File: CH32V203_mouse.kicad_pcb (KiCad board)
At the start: 2 copper layers, 30 parts, among them J1 USB_C_Receptacle_USB2.0_16P_u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, J2 Conn_01x05_Pin, J3 Conn_01x04_Pin, SW1 SW_Push, U1 CH32V203G6U6, U2 USBLC6-2SC6, U3 XC6206P332MR, X1 16MHz

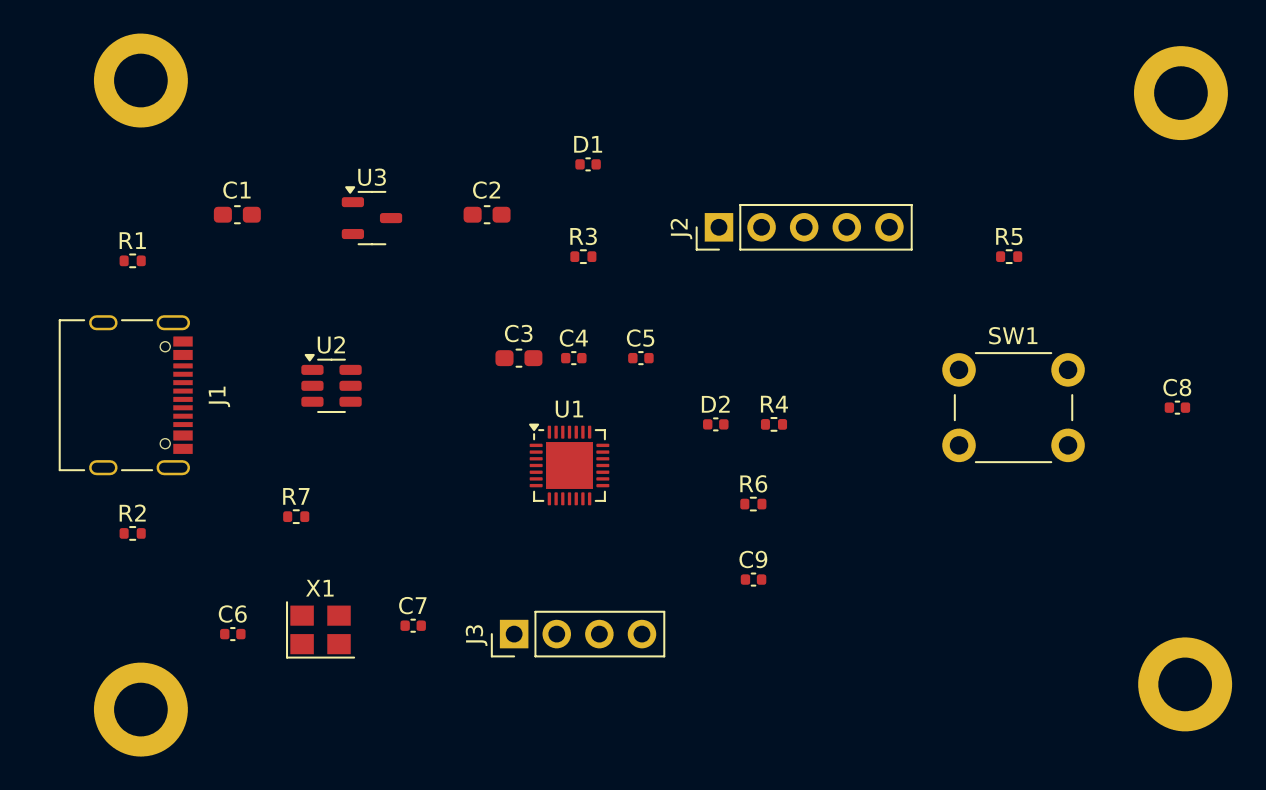
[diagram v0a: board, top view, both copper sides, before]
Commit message: Better PCB layout decoupling capacitors fixed changed LEDs footprints to correct ones
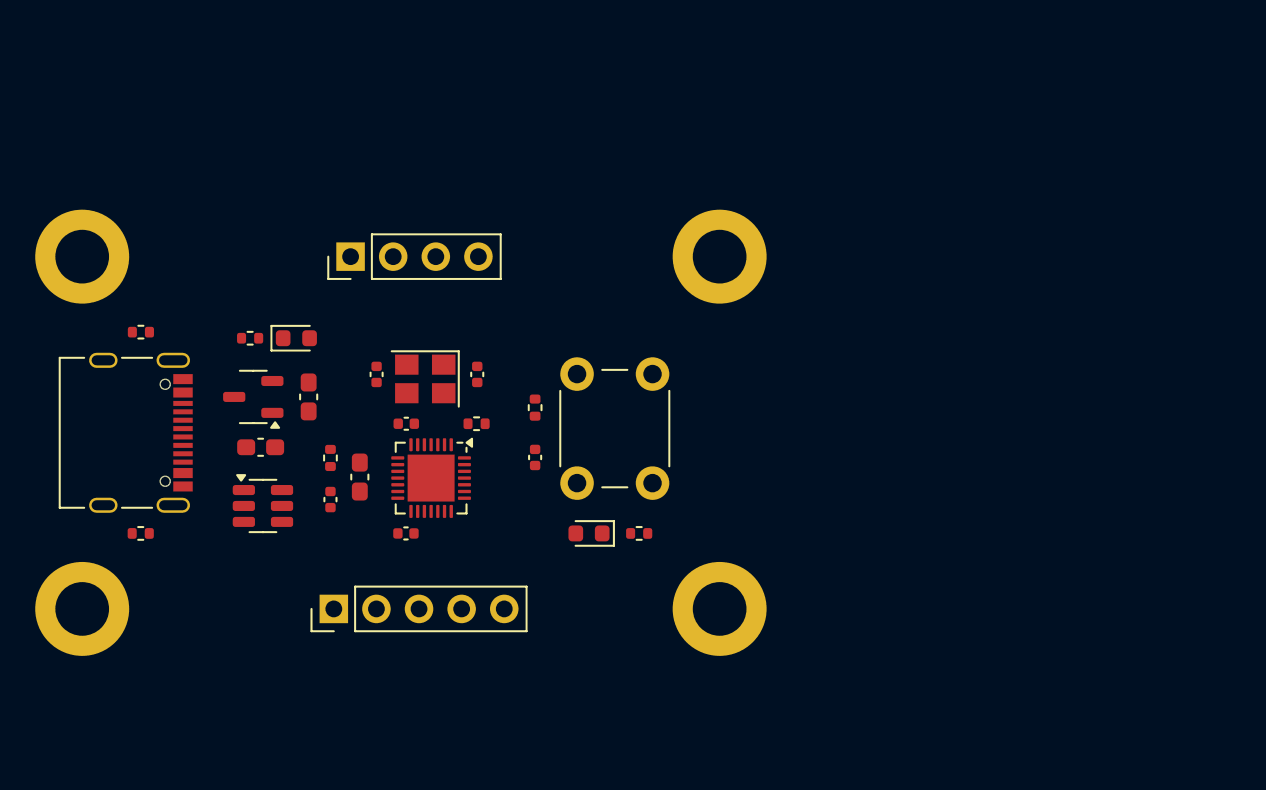
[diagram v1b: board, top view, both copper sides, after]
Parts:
- D1: footprint Capacitor_SMD:C_0402_1005Metric -> LED_SMD:LED_0603_1608Metric
- D2: footprint Capacitor_SMD:C_0402_1005Metric -> Diode_SMD:D_0603_1608Metric
- moved C8 38.4 mm to (147.0, 99.0), turned to -90 degrees
- moved J2 32.3 mm to (135.0, 108.0)
- moved R5 29.7 mm to (147.0, 96.0), turned to -90 degrees
- moved H2 29.2 mm to (158.0, 87.0)
- moved H4 28.1 mm to (158.0, 108.0)
- moved C9 25.7 mm to (134.8, 101.5), turned to -90 degrees
- moved R6 25.4 mm to (134.8, 99.0), turned to -90 degrees
- moved J3 24.5 mm to (136.0, 87.0)
- moved SW1 23.7 mm to (149.5, 100.5), turned to 90 degrees
- moved C6 21.3 mm to (143.6, 94.0), turned to -90 degrees
- moved R3 20.5 mm to (130.0, 91.9), turned to 180 degrees
- moved D1 20.2 mm to (132.8, 91.9)
- moved C5 17.5 mm to (139.3, 103.5), turned to 180 degrees
- moved X1 16.2 mm to (140.4, 94.3), turned to 180 degrees
- moved C2 15.2 mm to (133.5, 95.4), turned to -90 degrees
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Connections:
- C3 pad 2: /VDD -> GND
- C4 pad 2: /VDD -> GND
- C5 pad 2: /VDD -> GND
- U1 pad 17: /VDD -> +3.3V
- U1 pad 5: /VDD -> +3.3V

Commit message: Changed stack up to a 4-layer board
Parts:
- D2: footprint Diode_SMD:D_0603_1608Metric -> LED_SMD:LED_0603_1608Metric
- moved H2 5.00 mm to (153.0, 87.0)
- moved H4 5.00 mm to (153.0, 108.0)
- moved H1 2.00 mm to (122.0, 87.0)
- moved H3 2.00 mm to (122.0, 108.0)
- moved C8 0.75 mm to (146.2, 99.0)
- moved D2 0.75 mm to (149.5, 103.5)
- moved R4 0.75 mm to (152.5, 103.5)
- moved R5 0.75 mm to (146.2, 96.0)
- moved SW1 0.75 mm to (148.8, 100.5)
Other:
- copper layers 2 -> 4
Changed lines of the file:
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@@
 	(generator_version "8.0")
 	(general
-		(thickness 1.59)
+		(thickness 1.6062)
 		(legacy_teardrops no)
 	)
 	(paper "A4")
 	(layers
-		(0 "F.Cu" signal)
-		(31 "B.Cu" signal)
+		(0 "F.Cu" signal "Top.Cu")
+		(1 "In1.Cu" power "GND1.Cu")
+		(2 "In2.Cu" power "GND2.Cu")
+		(31 "B.Cu" signal "Bottom.Cu")
 		(32 "B.Adhes" user "B.Adhesive")
-		(33 "F.Adhes" user "F.Adhesive")
 		(34 "B.Paste" user)
 		(35 "F.Paste" user)
@@
 		(38 "B.Mask" user)
 		(39 "F.Mask" user)
-		(40 "Dwgs.User" user "User.Drawings")
-		(41 "Cmts.User" user "User.Comments")
 		(42 "Eco1.User" user "User.Eco1")
-		(43 "Eco2.User" user "User.Eco2")
 		(44 "Edge.Cuts" user)
 		(45 "Margin" user)
@@
 		(48 "B.Fab" user)
 		(49 "F.Fab" user)
-		(50 "User.1" user)
-		(51 "User.2" user)
-		(52 "User.3" user)
-		(53 "User.4" user)
-		(54 "User.5" user)
-		(55 "User.6" user)
-		(56 "User.7" user)
-		(57 "User.8" user)
-		(58 "User.9" user)
 	)
 	(setup
@@
 			)
 			(layer "dielectric 1"
+				(type "prepreg")
+				(thickness 0.2104)
+				(material "FR4")
+				(epsilon_r 4.5)
+				(loss_tangent 0.02)
+			)
+			(layer "In1.Cu"
+				(type "copper")
+				(thickness 0.0152)
+			)
+			(layer "dielectric 2"
 				(type "core")
-				(thickness 1.5)
+				(thickness 1.065)
+				(material "FR4")
+				(epsilon_r 4.5)
+				(loss_tangent 0.02)
+			)
+			(layer "In2.Cu"
+				(type "copper")
+				(thickness 0.0152)
+			)
+			(layer "dielectric 3"
+				(type "prepreg")
+				(thickness 0.2104)
 				(material "FR4")
 				(epsilon_r 4.5)
@@
 	(footprint "MountingHole:MountingHole_3.2mm_M3_DIN965_Pad"
 		(layer "F.Cu")
-		(at 120 87)
+		(at 122 87)
 		(descr "Mounting Hole 3.2mm, M3, DIN965")
 		(tags "mounting hole 3.2mm m3 din965")
@@
 	(footprint "MountingHole:MountingHole_3.2mm_M3_DIN965_Pad"
 		(layer "F.Cu")
-		(at 120 108)
+		(at 122 108)
 		(descr "Mounting Hole 3.2mm, M3, DIN965")
 		(tags "mounting hole 3.2mm m3 din965")
@@
 	(footprint "Resistor_SMD:R_0402_1005Metric"
 		(layer "F.Cu")
-		(at 153.2025 103.5)
+		(at 152.4525 103.5)
 		(descr "Resistor SMD 0402 (1005 Metric), square (rectangular) end terminal, IPC_7351 nominal, (Body size source: IPC-SM-782 page 72, https://www.pcb-3d.com/wordpress/wp-content/uploads/ipc-sm-782a_amendment_1_and_2.pdf), generated with kicad-footprint-generator")
 		(tags "resistor")
@@
 		)
 	)
-	(footprint "Diode_SMD:D_0603_1608Metric"
+	(footprint "LED_SMD:LED_0603_1608Metric"
 		(layer "F.Cu")
-		(at 150.2125 103.5 180)
-		(descr "Diode SMD 0603 (1608 Metric), square (rectangular) end terminal, IPC_7351 nominal, (Body size source: http://www.tortai-tech.com/upload/download/2011102023233369053.pdf), generated with kicad-footprint-generator")
-		(tags "diode")
+		(at 149.4625 103.5 180)
+		(descr "LED SMD 0603 (1608 Metric), square (rectangular) end terminal, IPC_7351 nominal, (Body size source: http://www.tortai-tech.com/upload/download/2011102023233369053.pdf), generated with kicad-footprint-generator")
+		(tags "LED")
 		(property "Reference" "D2"
-			(at 0 -1.43 0)
+			(at 0 -1.43 180)
 			(layer "F.SilkS")
 			(hide yes)
@@
 		)
 		(property "Value" "LED"
-			(at 0 1.43 0)
+			(at 0 1.43 180)
 			(layer "F.Fab")
 			(hide yes)
@@
 			)
 		)
-		(property "Footprint" "Diode_SMD:D_0603_1608Metric"
+		(property "Footprint" "LED_SMD:LED_0603_1608Metric"
 			(at 0 0 180)
 			(unlocked yes)
@@
 		)
 		(fp_text user "${REFERENCE}"
-			(at 0 0 360)
+			(at 0 0 180)
 			(layer "F.Fab")
 			(effects
@@
 			(pintype "passive")
 		)
-		(model "${KICAD8_3DMODEL_DIR}/Diode_SMD.3dshapes/D_0603_1608Metric.wrl"
+		(model "${KICAD8_3DMODEL_DIR}/LED_SMD.3dshapes/LED_0603_1608Metric.wrl"
 			(offset
 				(xyz 0 0 0)
@@
 	(footprint "Capacitor_SMD:C_0402_1005Metric"
 		(layer "F.Cu")
-		(at 147 98.97 -90)
+		(at 146.25 98.97 -90)
 		(descr "Capacitor SMD 0402 (1005 Metric), square (rectangular) end terminal, IPC_7351 nominal, (Body size source: IPC-SM-782 page 76, https://www.pcb-3d.com/wordpress/wp-content/uploads/ipc-sm-782a_amendment_1_and_2.pdf), generated with kicad-footprint-generator")
 		(tags "capacitor")
@@
 	(footprint "Button_Switch_THT:SW_PUSH_6mm_H4.3mm"
 		(layer "F.Cu")
-		(at 149.5 100.5 90)
+		(at 148.75 100.5 90)
 		(descr "tactile push button, 6x6mm e.g. PHAP33xx series, height=4.3mm")
 		(tags "tact sw push 6mm")
@@
 	(footprint "MountingHole:MountingHole_3.2mm_M3_DIN965_Pad"
 		(layer "F.Cu")
-		(at 158 87)
+		(at 153 87)
 		(descr "Mounting Hole 3.2mm, M3, DIN965")
 		(tags "mounting hole 3.2mm m3 din965")
@@
 	(footprint "MountingHole:MountingHole_3.2mm_M3_DIN965_Pad"
 		(layer "F.Cu")
-		(at 158 108)
+		(at 153 108)
 		(descr "Mounting Hole 3.2mm, M3, DIN965")
 		(tags "mounting hole 3.2mm m3 din965")
@@
 	(footprint "Resistor_SMD:R_0402_1005Metric"
 		(layer "F.Cu")
-		(at 147 96 -90)
+		(at 146.25 96 -90)
 		(descr "Resistor SMD 0402 (1005 Metric), square (rectangular) end terminal, IPC_7351 nominal, (Body size source: IPC-SM-782 page 72, https://www.pcb-3d.com/wordpress/wp-content/uploads/ipc-sm-782a_amendment_1_and_2.pdf), generated with kicad-footprint-generator")
 		(tags "resistor")

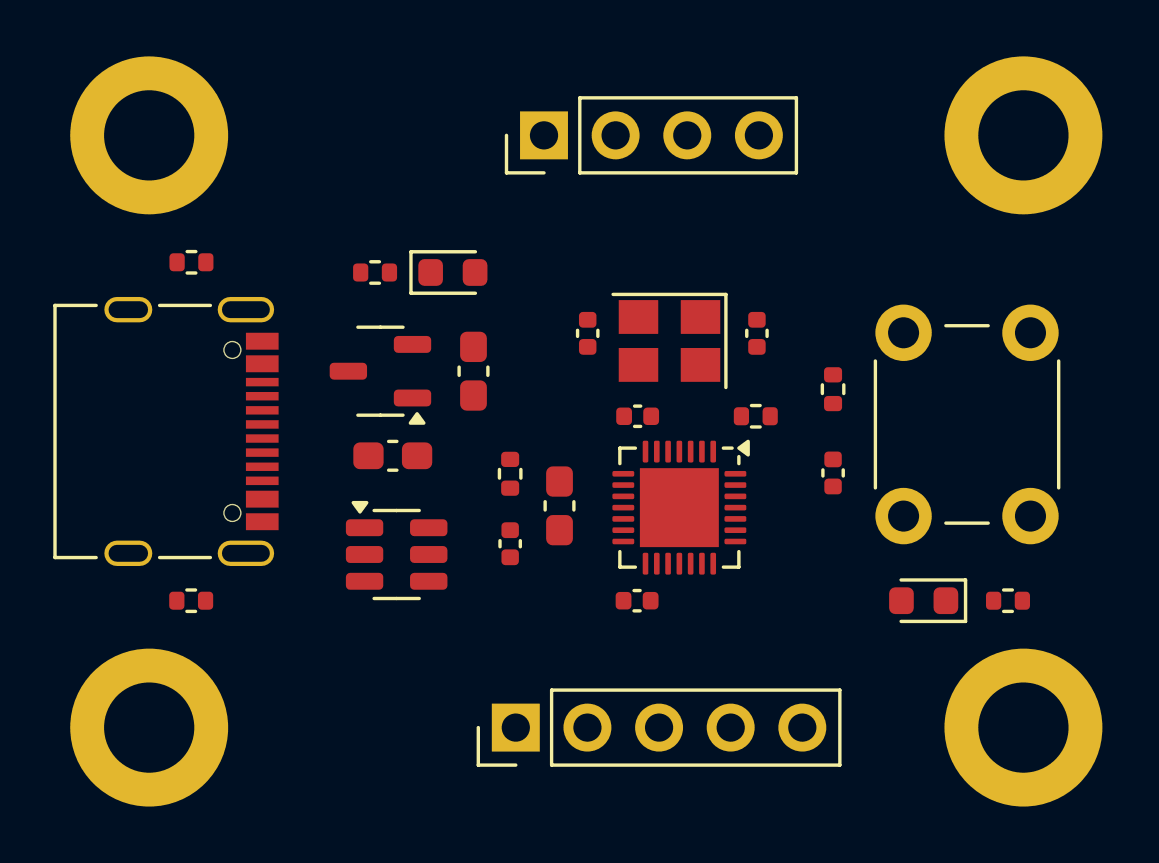
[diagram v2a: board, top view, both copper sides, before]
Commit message: Signals routed Constraints updated USB labels fixed
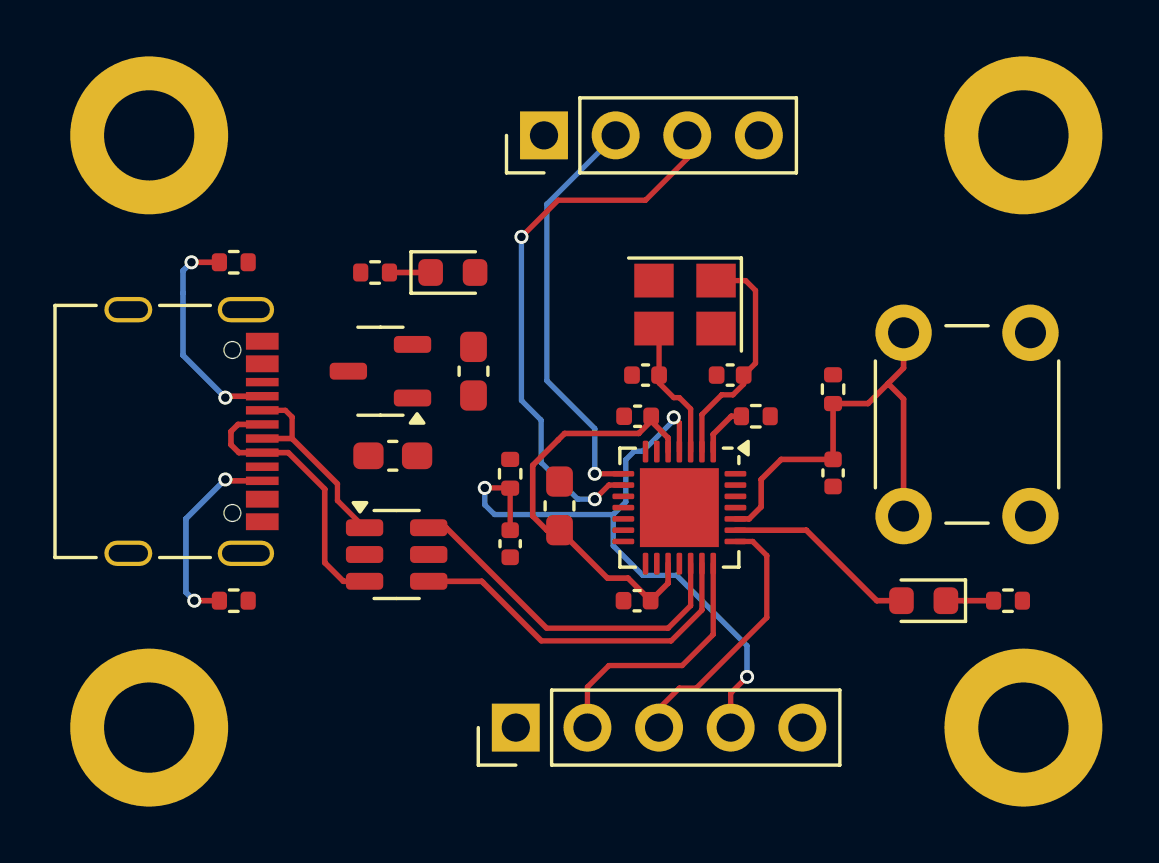
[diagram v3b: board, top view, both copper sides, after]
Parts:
- moved C7 2.53 mm to (139.6, 95.5), turned to 180 degrees
- moved C6 1.76 mm to (142.6, 95.5), turned to 180 degrees
- moved R2 1.51 mm to (125.0, 103.5)
- moved R1 1.50 mm to (125.0, 91.5)
- moved X1 1.40 mm to (141.0, 93.0)
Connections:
- net /USB_DM renamed /USB_DN
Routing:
- net /NRST: track 0.00 -> 24.0 mm, vias 0 -> 3
- net /UART_RX: track 0.00 -> 19.8 mm, vias 0 -> 2
- net /SWITCH: track 0.00 -> 16.1 mm
- net +3.3V: track 0.00 -> 15.1 mm
- net /UART_TX: track 0.00 -> 14.7 mm, vias 0 -> 1
- net /USB_DP: track 0.00 -> 12.7 mm
- net /USB_DN: track 0.00 -> 12.6 mm
- net /USB_conn+: track 0.00 -> 9.96 mm
- net /SWCLK: track 0.00 -> 9.35 mm
- net /SWDIO: track 0.00 -> 9.18 mm
- net /OSC_IN: track 0.00 -> 8.28 mm
- net /CC1: track 0.00 -> 7.87 mm, vias 0 -> 2
- net /CC2: track 0.00 -> 7.37 mm, vias 0 -> 2
- net /USB_conn-: track 0.00 -> 7.20 mm
- net /LED: track 0.00 -> 6.92 mm
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
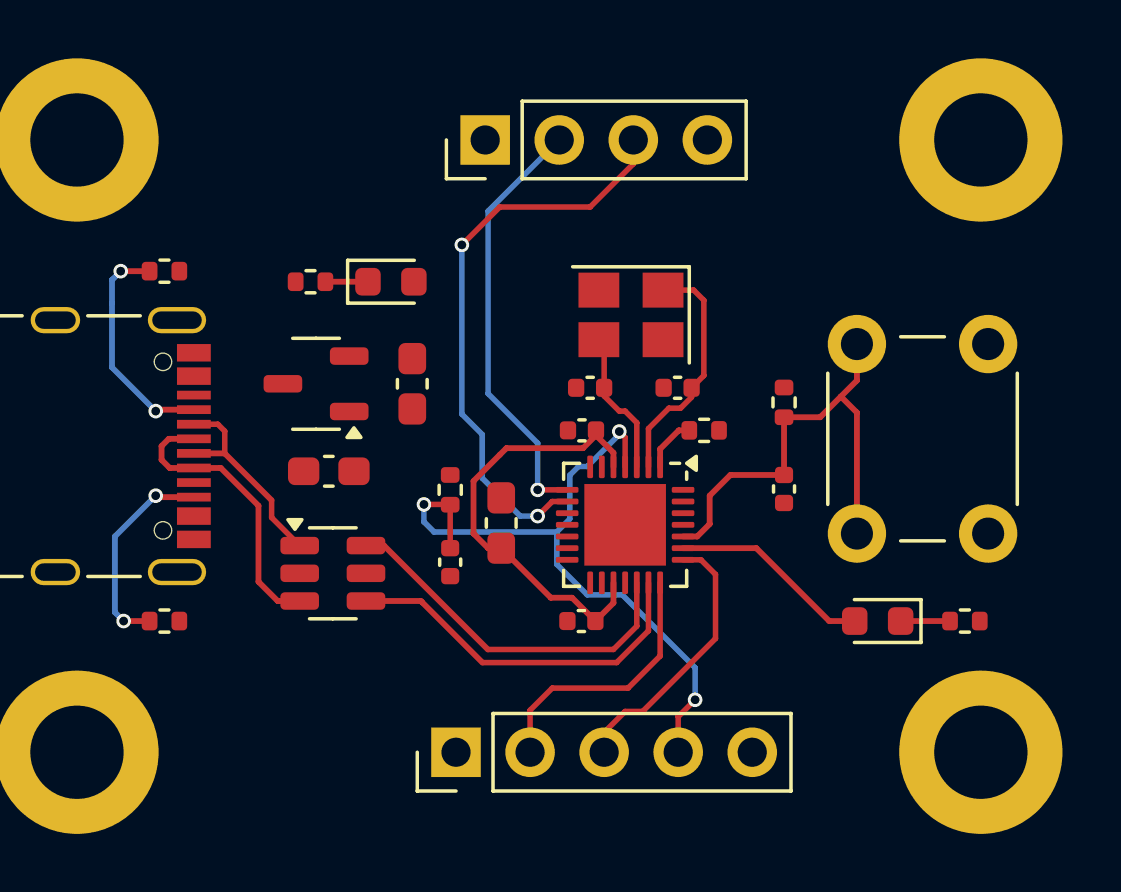
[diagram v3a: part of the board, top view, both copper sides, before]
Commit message: Power routing GND vias
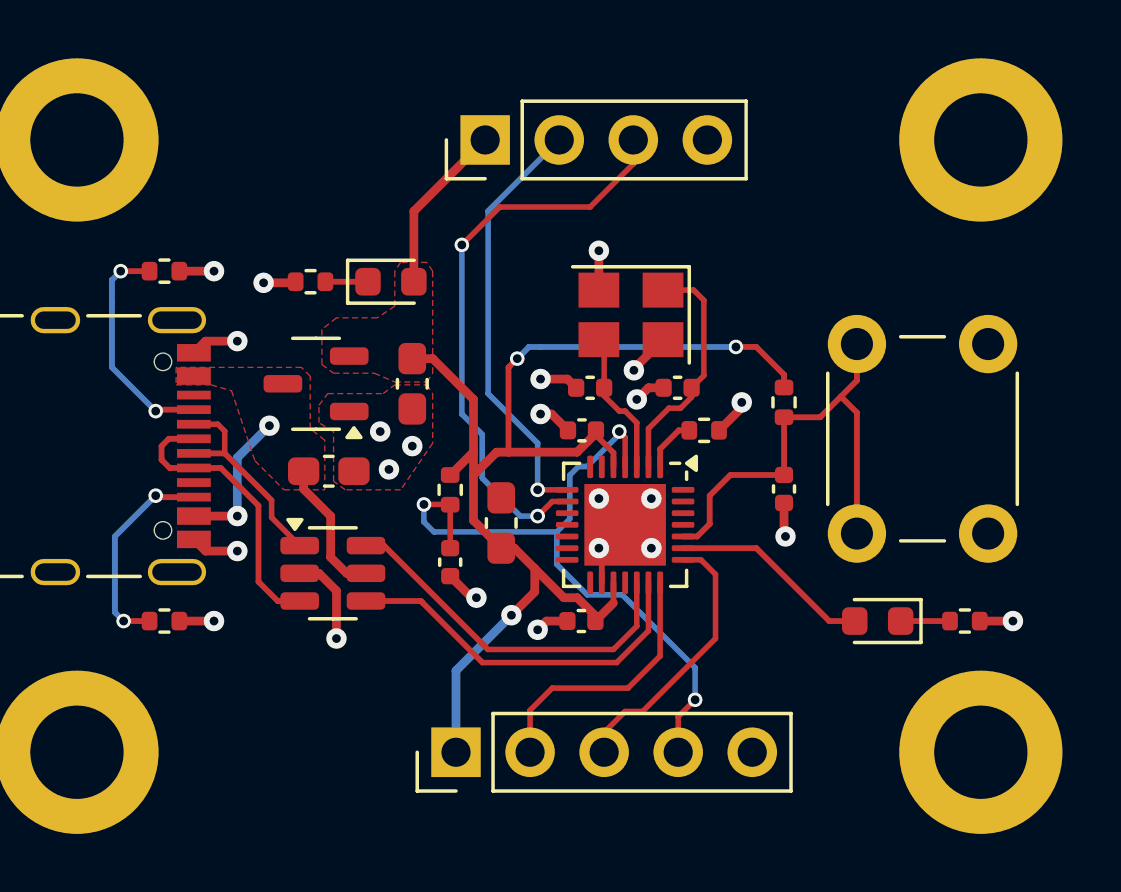
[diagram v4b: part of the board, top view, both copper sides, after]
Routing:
- net +3.3V: track 15.1 -> 48.4 mm, vias 0 -> 3
- net GND: track 0.00 -> 24.6 mm, vias 0 -> 23
- net VBUS: track 0.00 -> 9.82 mm, vias 0 -> 2
- added copper zone on F.Cu, net +3.3V
- added copper zone on F.Cu, net GND
- added copper zone on F.Cu, net VBUS
